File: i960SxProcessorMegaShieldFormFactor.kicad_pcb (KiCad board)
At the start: 4 copper layers, 101.6 x 53.3 mm, 44 parts, among them P1 Power, P2 Data Lines Lower, P3 Data Lines Upper, P4 Address Lines, P5 PWM, P6 Serializable Pins, P7 1284p Direct Connection, U1 74HC245, U2 74HC245, U3 80960Sx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

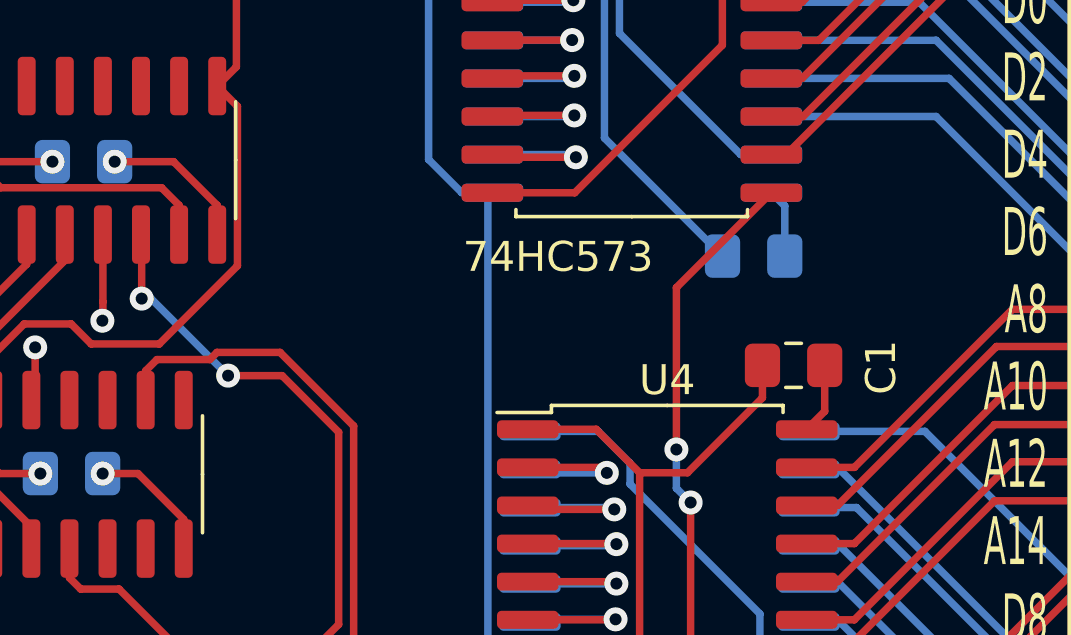
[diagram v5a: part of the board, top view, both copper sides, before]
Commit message: Finish wiring the last two non power pins
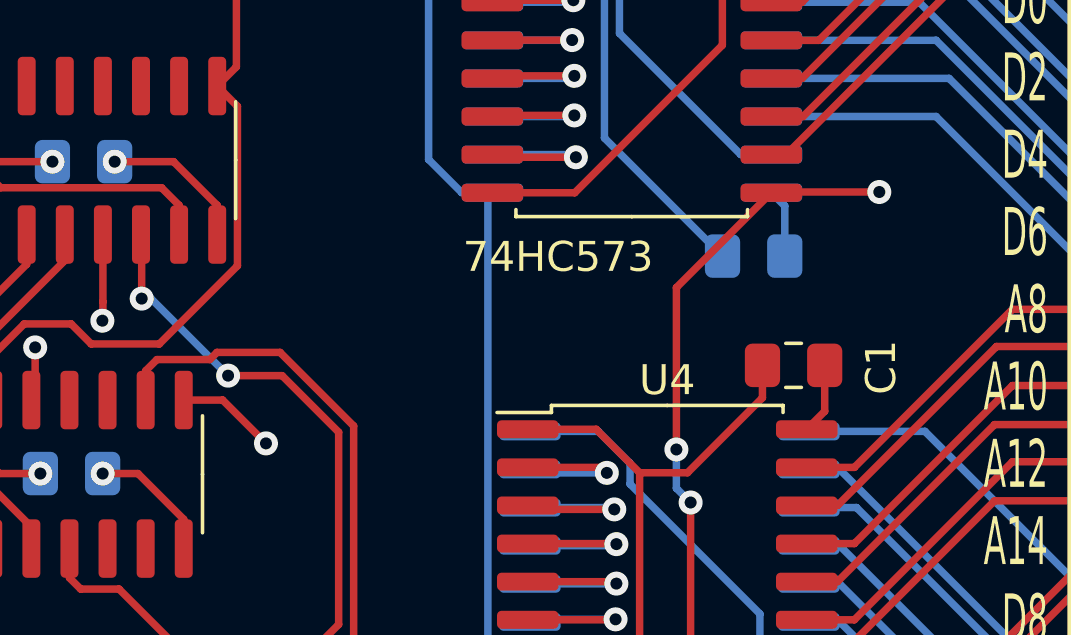
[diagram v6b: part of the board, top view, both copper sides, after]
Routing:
- net /ALE: track 50.0 -> 121.6 mm, vias 2 -> 3
- net /~READY960: track 0.00 -> 61.5 mm, vias 0 -> 1
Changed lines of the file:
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@@
     (thickness 1.6)
     (drawings 10)
-    (tracks 944)
+    (tracks 963)
     (zones 0)
     (modules 44)
@@
   (segment (start 120.618601 80.094497) (end 119.686179 81.026919) (width 0.25) (layer In1.Cu) (net 61))
   (segment (start 137.414 70.866) (end 136.02299 72.25701) (width 0.25) (layer In1.Cu) (net 61))
+  (segment (start 138.80501 72.25701) (end 185.47497 72.25701) (width 0.25) (layer In2.Cu) (net 61))
+  (segment (start 137.414 70.866) (end 138.80501 72.25701) (width 0.25) (layer In2.Cu) (net 61))
+  (segment (start 189.74308 76.52512) (end 189.74308 89.8144) (width 0.25) (layer In2.Cu) (net 61))
+  (via (at 189.74308 89.8144) (size 0.8) (drill 0.4) (layers Front Back) (net 61))
+  (segment (start 185.47497 72.25701) (end 189.74308 76.52512) (width 0.25) (layer In2.Cu) (net 61))
+  (segment (start 186.16602 89.8144) (end 186.14062 89.8398) (width 0.25) (layer Front) (net 61))
+  (segment (start 189.74308 89.8144) (end 186.16602 89.8144) (width 0.25) (layer Front) (net 61))
   (segment (start 176.69537 89.99267) (end 176.85078 89.83726) (width 0.25) (layer Back) (net 62))
   (segment (start 176.69537 108.84753) (end 176.69537 89.99267) (width 0.25) (layer Back) (net 62))
@@
   (segment (start 158.51482 80.99044) (end 158.74746 80.7578) (width 0.25) (layer Front) (net 103))
   (segment (start 156.94838 80.99044) (end 158.51482 80.99044) (width 0.25) (layer Front) (net 103))
+  (via (at 169.29862 98.19386) (size 0.8) (drill 0.4) (layers Front Back) (net 104))
+  (segment (start 167.85486 96.7501) (end 169.29862 98.19386) (width 0.25) (layer Front) (net 104))
+  (segment (start 166.55796 96.7501) (end 167.85486 96.7501) (width 0.25) (layer Front) (net 104))
+  (segment (start 169.29862 98.19386) (end 167.92956 96.8248) (width 0.25) (layer In2.Cu) (net 104))
+  (segment (start 145.453777 86.106919) (end 118.078601 86.106919) (width 0.25) (layer In2.Cu) (net 104))
+  (segment (start 146.386199 87.039341) (end 145.453777 86.106919) (width 0.25) (layer In2.Cu) (net 104))
+  (segment (start 118.078601 86.106919) (end 116.9924 87.19312) (width 0.25) (layer In2.Cu) (net 104))
+  (segment (start 146.386199 87.714497) (end 146.386199 87.039341) (width 0.25) (layer In2.Cu) (net 104))
+  (segment (start 146.951023 88.279321) (end 146.386199 87.714497) (width 0.25) (layer In2.Cu) (net 104))
+  (segment (start 147.626179 88.279321) (end 146.951023 88.279321) (width 0.25) (layer In2.Cu) (net 104))
+  (segment (start 156.171658 96.8248) (end 147.626179 88.279321) (width 0.25) (layer In2.Cu) (net 104))
+  (segment (start 167.92956 96.8248) (end 156.171658 96.8248) (width 0.25) (layer In2.Cu) (net 104))
   (segment (start 166.36746 75.8078) (end 166.36746 76.931304) (width 0.25) (layer Front) (net 105))
   (segment (start 168.31247 78.876314) (end 168.31247 85.64331) (width 0.25) (layer Front) (net 105))

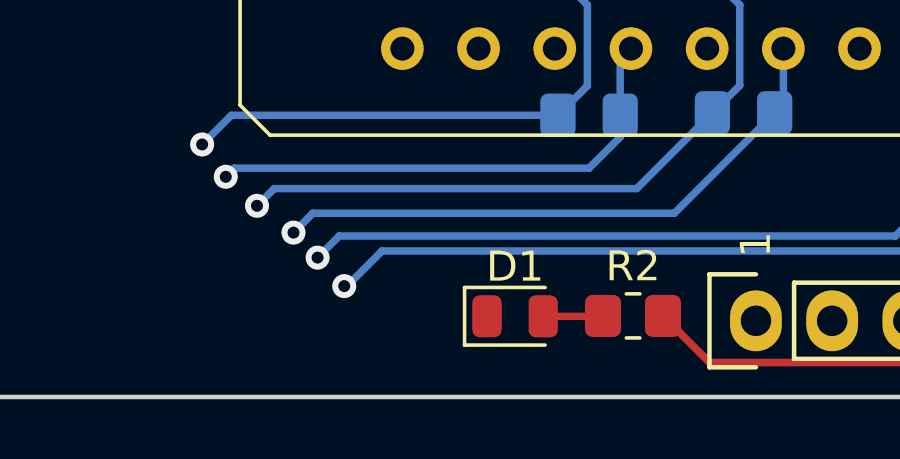
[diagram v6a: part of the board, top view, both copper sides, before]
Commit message: added a track for the 3.3v power led
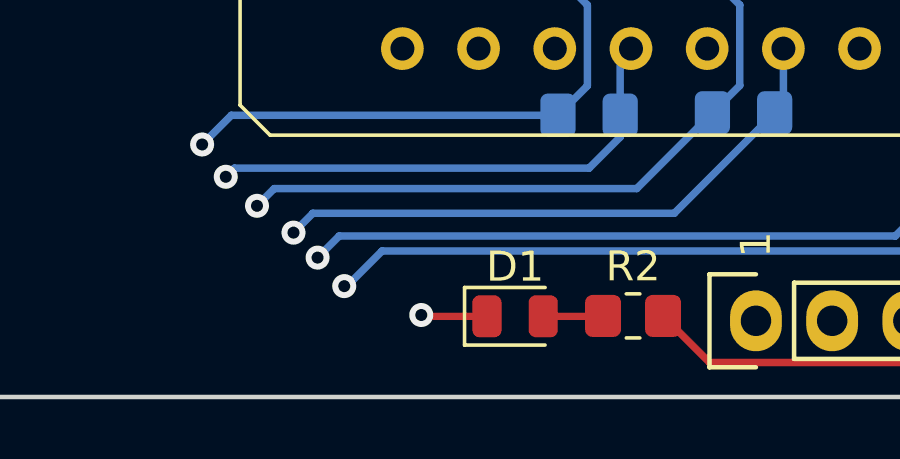
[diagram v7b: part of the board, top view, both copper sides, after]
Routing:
- net GND: track 229.2 -> 231.4 mm, vias 12 -> 13
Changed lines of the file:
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@@
     (thickness 1.6)
     (drawings 10)
-    (tracks 963)
+    (tracks 966)
     (zones 0)
     (modules 44)
@@
   (segment (start 180.581669 88.015089) (end 180.581669 80.711317) (width 0.25) (layer Back) (net 1))
   (segment (start 180.581669 80.711317) (end 178.277612 78.40726) (width 0.25) (layer Back) (net 1))
+  (via (at 120.16232 118.93296) (size 0.8) (drill 0.4) (layers Front Back) (net 1))
+  (segment (start 120.2055 118.97614) (end 120.16232 118.93296) (width 0.25) (layer Front) (net 1))
+  (segment (start 122.35156 118.97614) (end 120.2055 118.97614) (width 0.25) (layer Front) (net 1))
   (segment (start 186.59212 90.2786) (end 186.15078 89.83726) (width 0.25) (layer Back) (net 2))
   (segment (start 186.59212 91.95054) (end 186.59212 90.2786) (width 0.25) (layer Back) (net 2))

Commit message: Finished initial design
Still need to update the silk screens
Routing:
- net +5V: track 180.4 -> 251.0 mm, vias 11 -> 26
- net GND: track 231.4 -> 296.4 mm, vias 13 -> 23
- net /~DEN: track 75.0 -> 99.9 mm, vias 0 -> 2
- net /~BLAST~\~FAIL~: track 70.1 -> 69.5 mm
- added copper zone on F.Cu, net +5V
- added copper zone on B.Cu, net GND
